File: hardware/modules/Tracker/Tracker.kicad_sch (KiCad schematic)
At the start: 0 parts

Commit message: 諸々修正しました
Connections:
- no-connect marks 0 -> 7
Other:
- removed sheet GPS_Active
- added sheet GPSActive (../../components/GPSActive/GPSActive.kicad_sch)

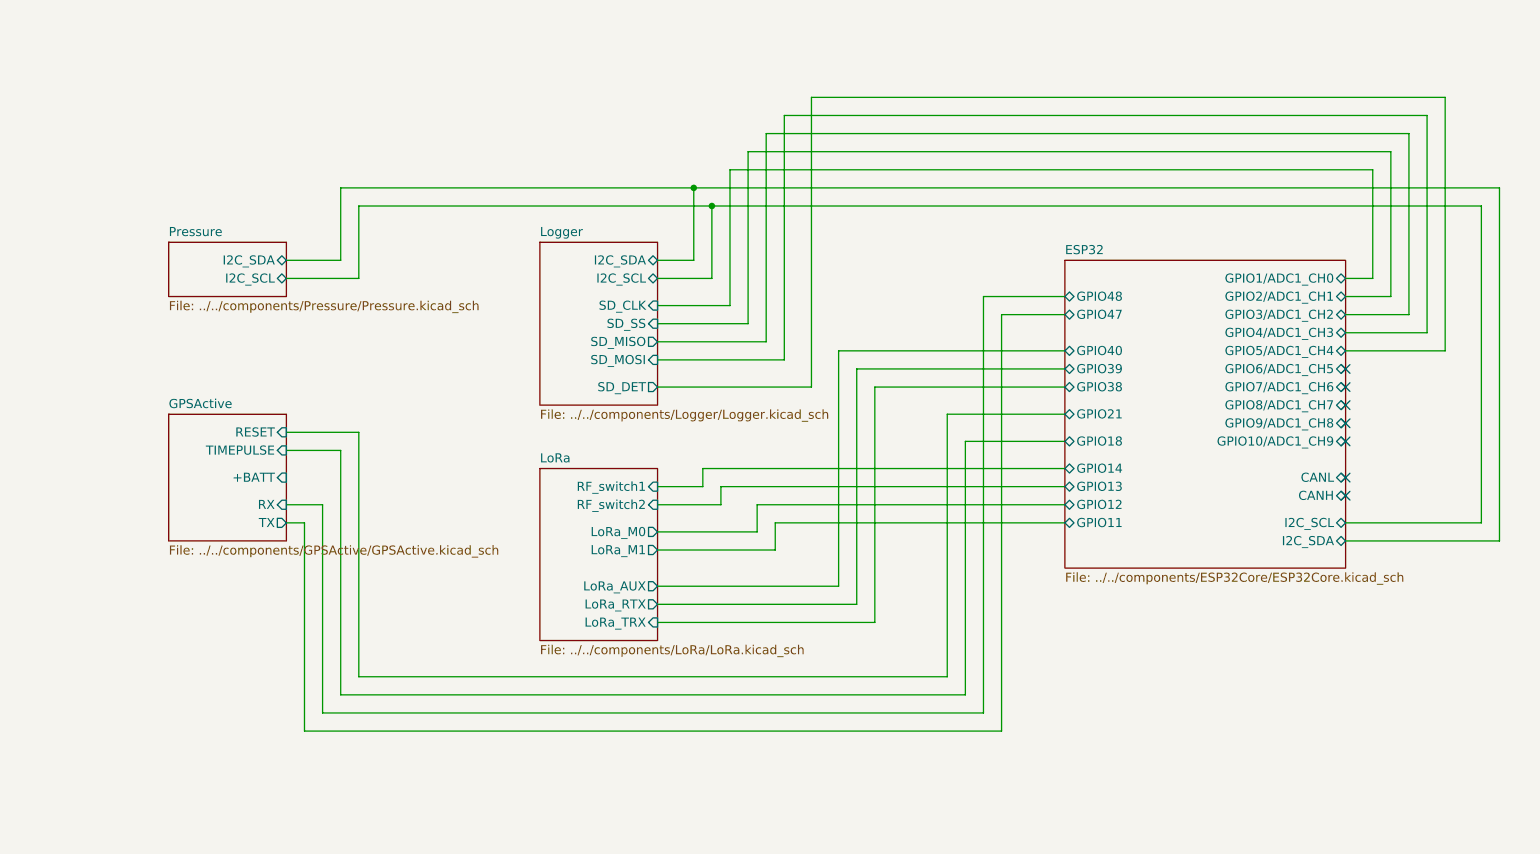
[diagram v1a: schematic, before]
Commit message: trackerにlipoを加え忘れてたので追加しました
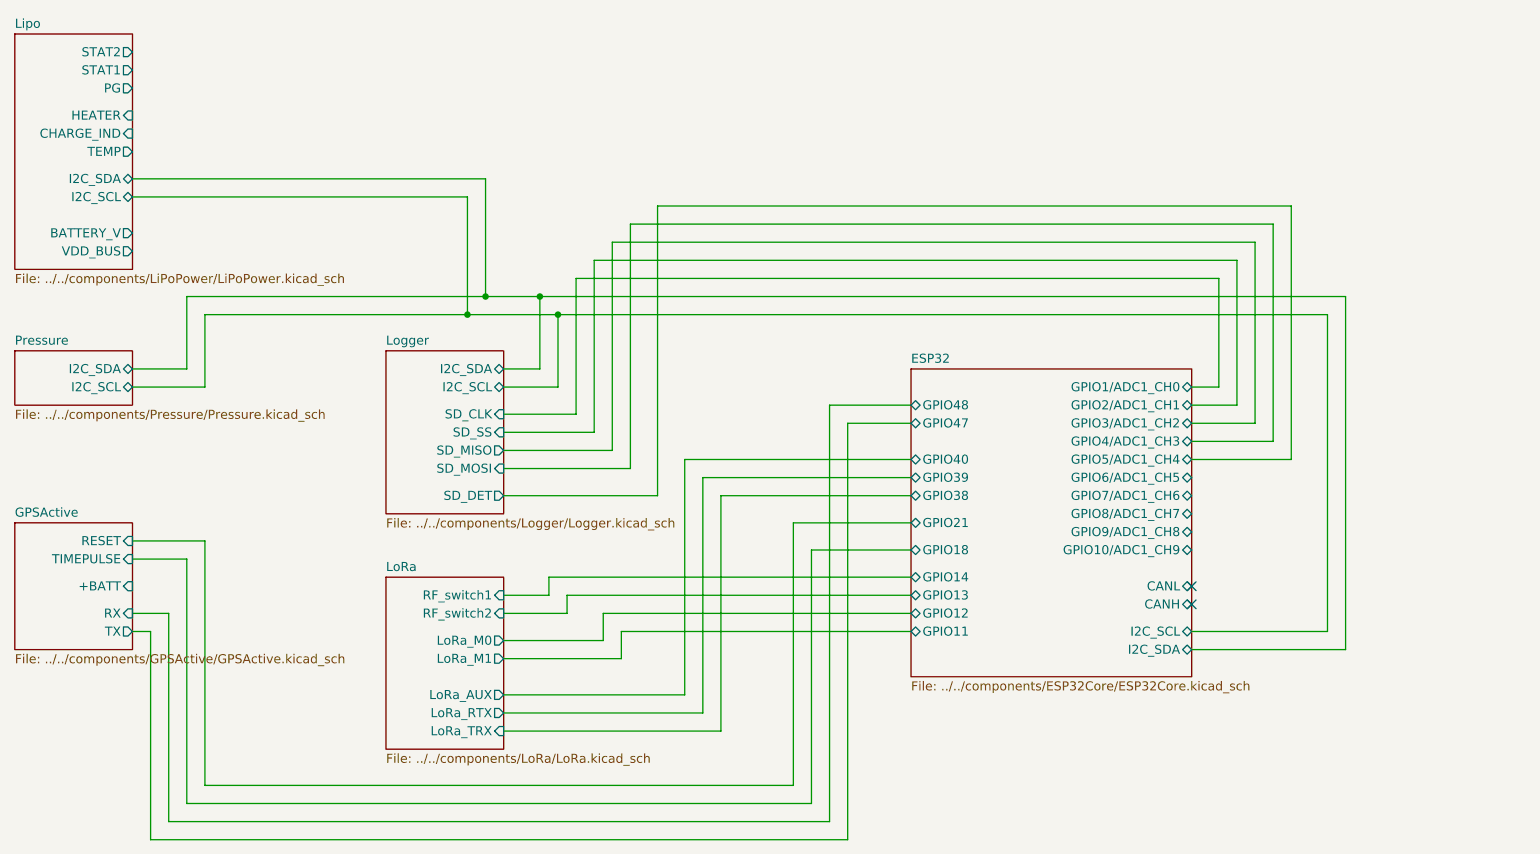
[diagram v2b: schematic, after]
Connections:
- no-connect marks 7 -> 2
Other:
- added sheet Lipo (../../components/LiPoPower/LiPoPower.kicad_sch)
